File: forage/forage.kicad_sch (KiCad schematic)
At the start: 68 parts, among them J1 Conn_01x04_MountingPin, Q1 AO3400A, U1 STM32G431RBTx, U2 XC6206P322MR

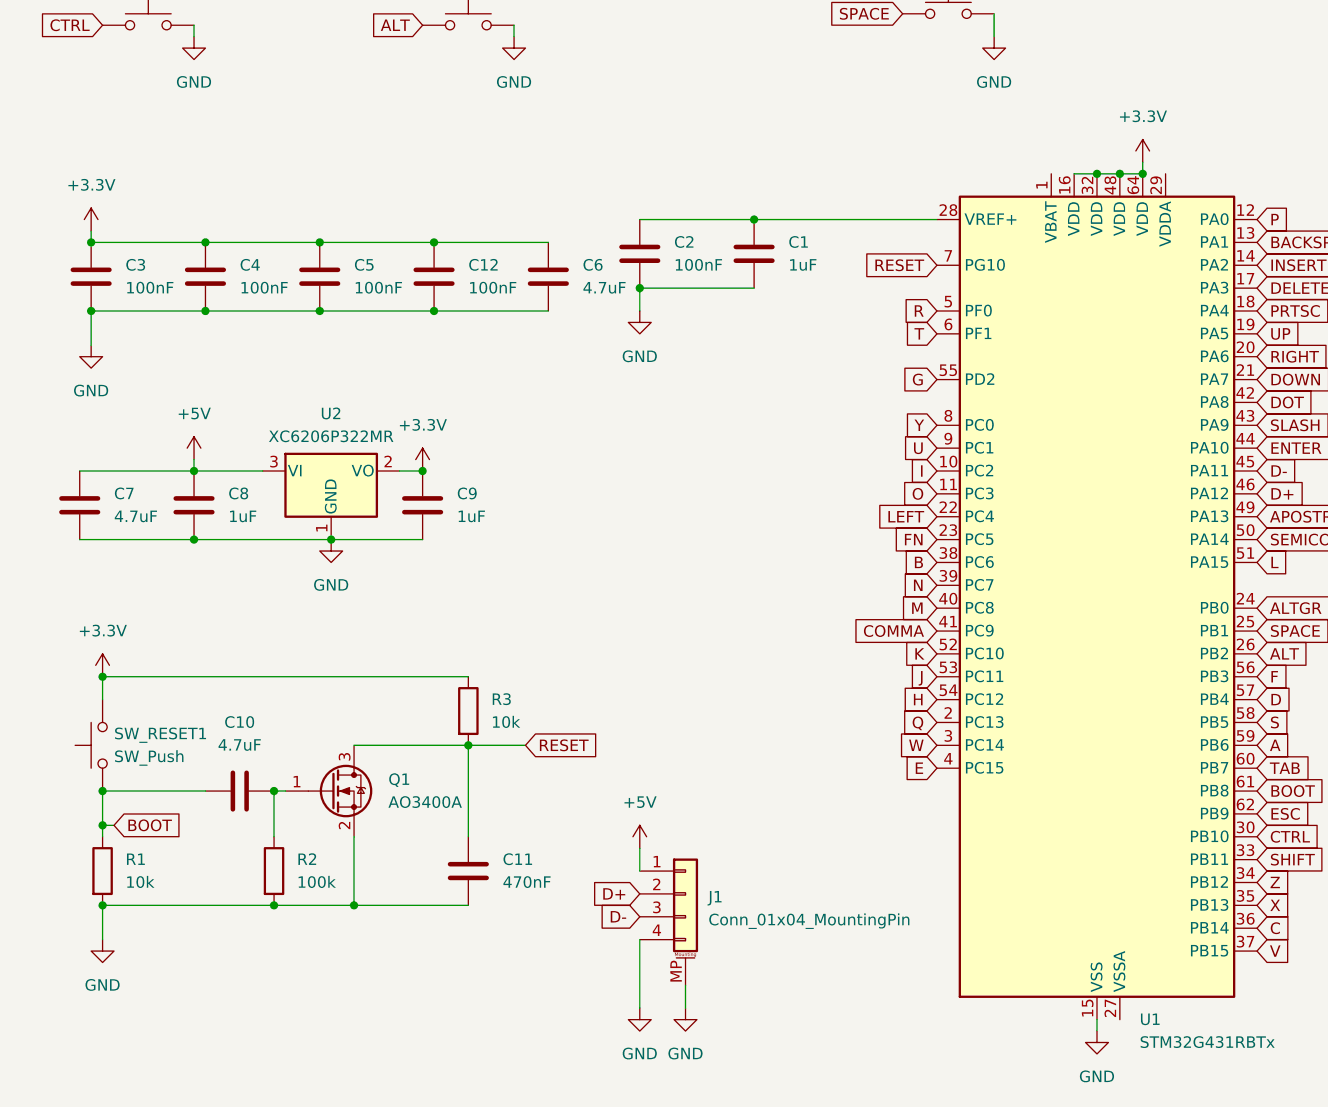
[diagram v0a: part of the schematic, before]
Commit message: move connector so D+/D- has a direct path
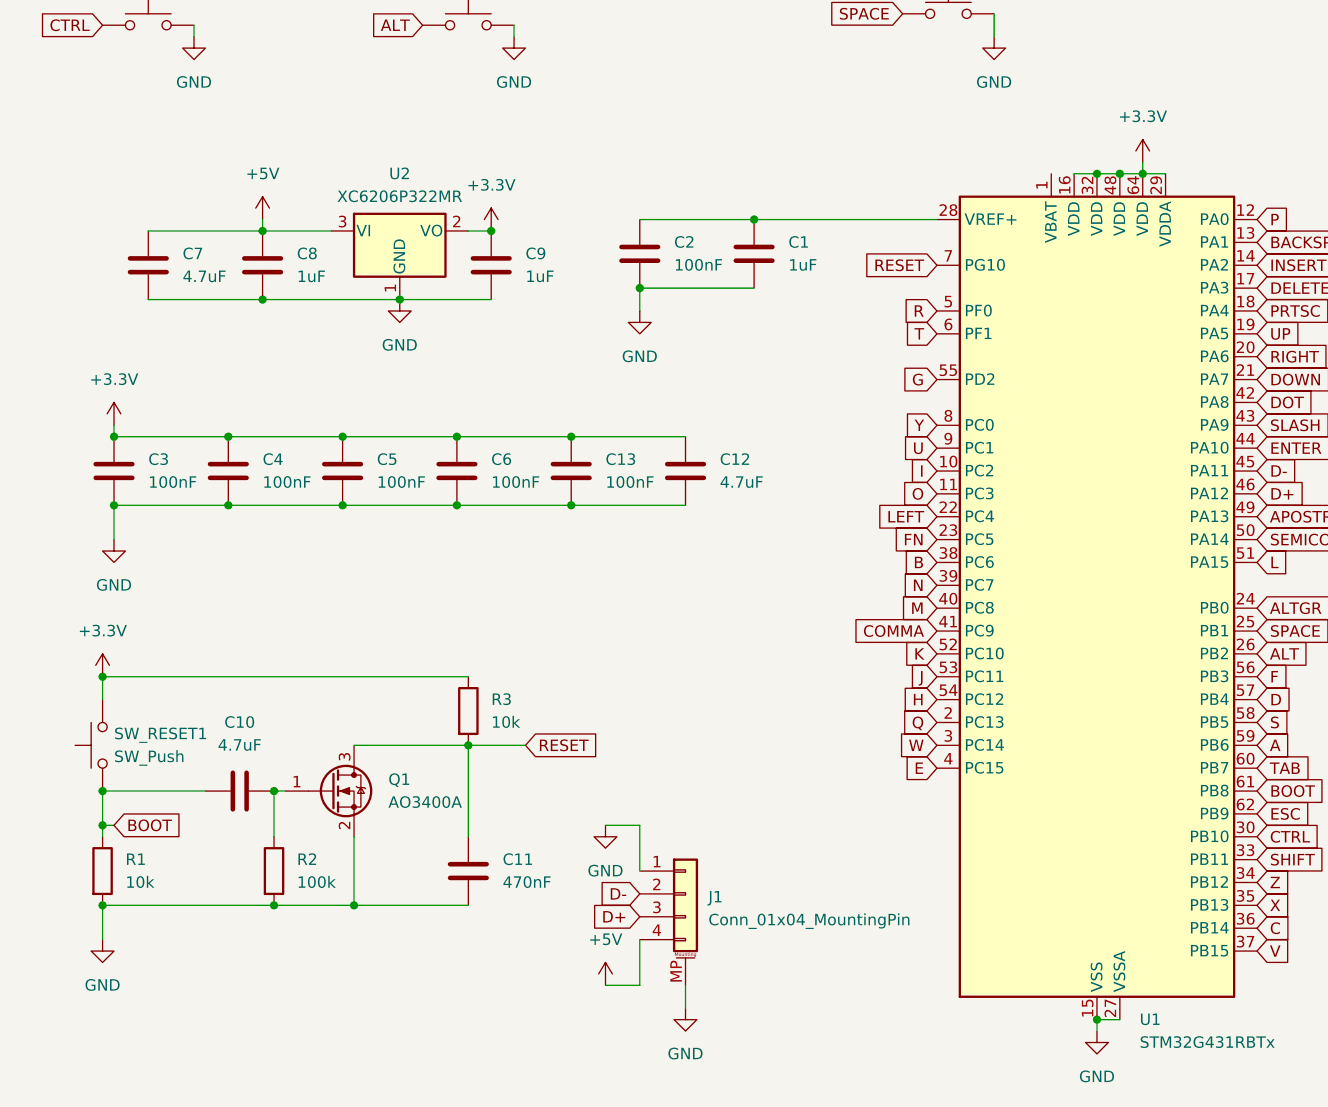
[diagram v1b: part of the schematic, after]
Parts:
- added C13: 100nF, Capacitor_SMD:C_0805_2012Metric, symbol Device:C
- C12: value 100nF -> 4.7uF
- C6: value 4.7uF -> 100nF
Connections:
- net +3.3V: now also U1.29 (VDDA), C13.1
- net +5V: now also J1.4 (Pin_4); no longer J1.1 (Pin_1)
- net D+: now also J1.3 (Pin_3); no longer J1.2 (Pin_2)
- net D-: now also J1.2 (Pin_2); no longer J1.3 (Pin_3)
- net GND: now also J1.1 (Pin_1), U1.27 (VSSA), C13.2; no longer J1.4 (Pin_4)
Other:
- moved on the sheet: C7, C8, C9, U2

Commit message: wip: v2
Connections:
- net APOSTROPHE: now also U1.50 (PA14); no longer U1.49 (PA13)
- net SEMICOLON: now also U1.49 (PA13); no longer U1.50 (PA14)

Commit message: fix connector pins.... i think!
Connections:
- net +5V: now also J1.1 (Pin_1); no longer J1.4 (Pin_4)
- net GND: now also J1.4 (Pin_4); no longer J1.1 (Pin_1)
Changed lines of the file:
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@@
 	(wire
 		(pts
+			(xy 83.82 170.18) (xy 83.82 173.99)
+		)
+		(stroke
+			(width 0)
+			(type default)
+		)
+	)
+	(wire
+		(pts
 			(xy 134.62 190.5) (xy 137.16 190.5)
 		)
@@
 	(wire
 		(pts
-			(xy 80.01 168.91) (xy 83.82 168.91)
-		)
-		(stroke
-			(width 0)
-			(type default)
-		)
-	)
-	(wire
-		(pts
 			(xy 52.07 177.8) (xy 64.77 177.8)
 		)
@@
 	(wire
 		(pts
-			(xy 83.82 168.91) (xy 83.82 173.99)
-		)
-		(stroke
-			(width 0)
-			(type default)
-		)
-	)
-	(wire
-		(pts
 			(xy 137.16 96.52) (xy 139.7 96.52)
 		)
@@
 	(wire
 		(pts
-			(xy 83.82 186.69) (xy 80.01 186.69)
-		)
-		(stroke
-			(width 0)
-			(type default)
-		)
-	)
-	(wire
-		(pts
 			(xy 76.2 133.35) (xy 88.9 133.35)
 		)
@@
 		)
 	)
+	(global_label "D+"
+		(shape input)
+		(at 83.82 179.07 180)
+		(fields_autoplaced yes)
+		(effects
+			(font
+				(size 1.27 1.27)
+			)
+			(justify right)
+		)
+		(property "Intersheetrefs" "${INTERSHEET_REFS}"
+			(at 77.9924 179.07 0)
+			(effects
+				(font
+					(size 1.27 1.27)
+				)
+				(justify right)
+				(hide yes)
+			)
+		)
+	)
 	(global_label "SPACE"
 		(shape input)
@@
 		)
 	)
-	(global_label "D-"
-		(shape input)
-		(at 83.82 176.53 180)
-		(fields_autoplaced yes)
-		(effects
-			(font
-				(size 1.27 1.27)
-			)
-			(justify right)
-		)
-		(property "Intersheetrefs" "${INTERSHEET_REFS}"
-			(at 77.9924 176.53 0)
-			(effects
-				(font
-					(size 1.27 1.27)
-				)
-				(justify right)
-				(hide yes)
-			)
-		)
-	)
 	(global_label "BACKSPACE"
 		(shape input)
@@
 		)
 	)
-	(global_label "D+"
+	(global_label "D-"
 		(shape input)
-		(at 83.82 179.07 180)
+		(at 83.82 176.53 180)
 		(fields_autoplaced yes)
 		(effects
@@
 		)
 		(property "Intersheetrefs" "${INTERSHEET_REFS}"
-			(at 77.9924 179.07 0)
+			(at 77.9924 176.53 0)
 			(effects
 				(font
@@
 	)
 	(symbol
-		(lib_id "power:+5V")
-		(at 80.01 186.69 0)
-		(unit 1)
-		(exclude_from_sim no)
-		(in_bom yes)
-		(on_board yes)
-		(dnp no)
-		(fields_autoplaced yes)
-		(property "Reference" "#PWR056"
-			(at 80.01 190.5 0)
-			(effects
-				(font
-					(size 1.27 1.27)
-				)
-				(hide yes)
-			)
-		)
-		(property "Value" "+5V"
-			(at 80.01 181.61 0)
-			(effects
-				(font
-					(size 1.27 1.27)
-				)
-			)
-		)
-		(property "Footprint" ""
-			(at 80.01 186.69 0)
-			(effects
-				(font
-					(size 1.27 1.27)
-				)
-				(hide yes)
-			)
-		)
-		(property "Datasheet" ""
-			(at 80.01 186.69 0)
-			(effects
-				(font
-					(size 1.27 1.27)
-				)
-				(hide yes)
-			)
-		)
-		(property "Description" "Power symbol creates a global label with name \"+5V\""
-			(at 80.01 186.69 0)
-			(effects
-				(font
-					(size 1.27 1.27)
-				)
-				(hide yes)
-			)
-		)
-		(pin "1"
-		)
-		(instances
-			(project "forage"
-				(path "/50ca4619-510e-49f7-b5dd-5e04cd25f096"
-					(reference "#PWR056")
-					(unit 1)
-				)
-			)
-		)
-	)
-	(symbol
 		(lib_id "Switch:SW_Push")
 		(at 240.03 77.47 0)
@@
 	)
 	(symbol
+		(lib_id "power:+5V")
+		(at 83.82 170.18 0)
+		(unit 1)
+		(exclude_from_sim no)
+		(in_bom yes)
+		(on_board yes)
+		(dnp no)
+		(property "Reference" "#PWR056"
+			(at 83.82 173.99 0)
+			(effects
+				(font
+					(size 1.27 1.27)
+				)
+				(hide yes)
+			)
+		)
+		(property "Value" "+5V"
+			(at 83.82 165.1 0)
+			(effects
+				(font
+					(size 1.27 1.27)
+				)
+			)
+		)
+		(property "Footprint" ""
+			(at 83.82 170.18 0)
+			(effects
+				(font
+					(size 1.27 1.27)
+				)
+				(hide yes)
+			)
+		)
+		(property "Datasheet" ""
+			(at 83.82 170.18 0)
+			(effects
+				(font
+					(size 1.27 1.27)
+				)
+				(hide yes)
+			)
+		)
+		(property "Description" "Power symbol creates a global label with name \"+5V\""
+			(at 83.82 170.18 0)
+			(effects
+				(font
+					(size 1.27 1.27)
+				)
+				(hide yes)
+			)
+		)
+		(pin "1"
+		)
+		(instances
+			(project "forage"
+				(path "/50ca4619-510e-49f7-b5dd-5e04cd25f096"
+					(reference "#PWR056")
+					(unit 1)
+				)
+			)
+		)
+	)
+	(symbol
 		(lib_id "power:GND")
 		(at 220.98 46.99 0)
@@
 	)
 	(symbol
-		(lib_id "power:GND")
-		(at 80.01 168.91 0)
-		(unit 1)
-		(exclude_from_sim no)
-		(in_bom yes)
-		(on_board yes)
-		(dnp no)
-		(property "Reference" "#PWR051"
-			(at 80.01 175.26 0)
-			(effects
-				(font
-					(size 1.27 1.27)
-				)
-				(hide yes)
-			)
-		)
-		(property "Value" "GND"
-			(at 80.01 173.99 0)
-			(effects
-				(font
-					(size 1.27 1.27)
-				)
-			)
-		)
-		(property "Footprint" ""
-			(at 80.01 168.91 0)
-			(effects
-				(font
-					(size 1.27 1.27)
-				)
-				(hide yes)
-			)
-		)
-		(property "Datasheet" ""
-			(at 80.01 168.91 0)
-			(effects
-				(font
-					(size 1.27 1.27)
-				)
-				(hide yes)
-			)
-		)
-		(property "Description" "Power symbol creates a global label with name \"GND\" , ground"
-			(at 80.01 168.91 0)
-			(effects
-				(font
-					(size 1.27 1.27)
-				)
-				(hide yes)
-			)
-		)
-		(pin "1"
-		)
-		(instances
-			(project "forage"
-				(path "/50ca4619-510e-49f7-b5dd-5e04cd25f096"
-					(reference "#PWR051")
-					(unit 1)
-				)
-			)
-		)
-	)
-	(symbol
 		(lib_id "Switch:SW_Push")
 		(at 172.72 29.21 0)
@@
 					(unit 1)
 				)
+			)
+		)
+	)
+	(symbol
+		(lib_id "power:GND")
+		(at 83.82 186.69 0)
+		(unit 1)
+		(exclude_from_sim no)
+		(in_bom yes)
+		(on_board yes)
+		(dnp no)
+		(property "Reference" "#PWR051"
+			(at 83.82 193.04 0)
+			(effects
+				(font
+					(size 1.27 1.27)
+				)
+				(hide yes)
+			)
+		)
+		(property "Value" "GND"
+			(at 83.82 191.77 0)
+			(effects
+				(font
+					(size 1.27 1.27)
+				)
+			)
+		)
+		(property "Footprint" ""
+			(at 83.82 186.69 0)
+			(effects
+				(font
+					(size 1.27 1.27)
+				)
+				(hide yes)
+			)
+		)
+		(property "Datasheet" ""
+			(at 83.82 186.69 0)
+			(effects
+				(font
+					(size 1.27 1.27)
+				)
+				(hide yes)
+			)
+		)
+		(property "Description" "Power symbol creates a global label with name \"GND\" , ground"
+			(at 83.82 186.69 0)
+			(effects
+				(font
+					(size 1.27 1.27)
+				)
+				(hide yes)
+			)
+		)
+		(pin "1"
+		)
+		(instances
+			(project "forage"
+				(path "/50ca4619-510e-49f7-b5dd-5e04cd25f096"
+					(reference "#PWR051")
+					(unit 1)
+				)

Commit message: switch to jst
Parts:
- J1: footprint Connector_Molex:Molex_Pico-EZmate_78171-0004_1x04-1MP_P1.20mm_Vertical -> Connector_JST:JST_SH_SM04B-SRSS-TB_1x04-1MP_P1.00mm_Horizontal
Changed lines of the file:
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@@
 			)
 		)
-		(property "Footprint" "Connector_Molex:Molex_Pico-EZmate_78171-0004_1x04-1MP_P1.20mm_Vertical"
+		(property "Footprint" "Connector_JST:JST_SH_SM04B-SRSS-TB_1x04-1MP_P1.00mm_Horizontal"
 			(at 88.9 176.53 0)
 			(effects

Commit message: correct xc6206 thingy
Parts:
- U2: value XC6206P322MR -> XC6206P332MR
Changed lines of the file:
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@@
 			)
 		)
-		(property "Value" "XC6206P322MR"
+		(property "Value" "XC6206P332MR"
 			(at 57.15 99.06 0)
 			(effects

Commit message: connect vbat to the 3.3v net
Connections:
- net +3.3V: now also U1.1 (VBAT)
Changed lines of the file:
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@@
+	)
+	(junction
+		(at 132.08 96.52)
+		(diameter 0)
+		(color 0 0 0 0)
 	)
 	(junction
@@
 		)
 		(stroke
+			(width 0)
+			(type default)
+		)
+	)
+	(wire
+		(pts
+			(xy 129.54 96.52) (xy 132.08 96.52)
+		)
+		(stroke

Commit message: recommended schmeccomended??? ok
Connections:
- net +3.3V: no longer U1.1 (VBAT)
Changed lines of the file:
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@@
-	)
-	(junction
-		(at 132.08 96.52)
-		(diameter 0)
-		(color 0 0 0 0)
 	)
 	(junction
@@
 		)
 		(stroke
-			(width 0)
-			(type default)
-		)
-	)
-	(wire
-		(pts
-			(xy 129.54 96.52) (xy 132.08 96.52)
-		)
-		(stroke
